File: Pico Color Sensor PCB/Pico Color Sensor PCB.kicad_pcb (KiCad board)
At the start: 2 copper layers, 62.2 x 80.4 mm, 13 parts

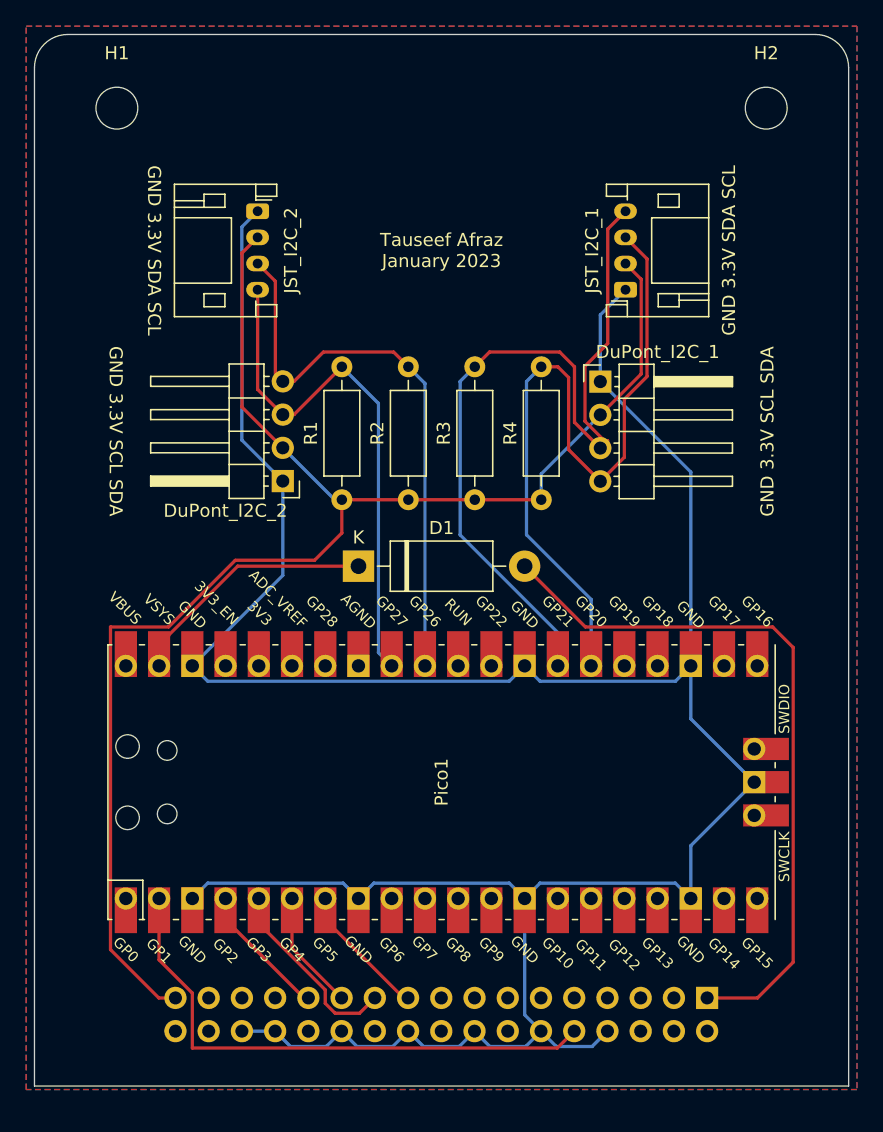
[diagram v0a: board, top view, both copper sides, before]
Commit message: Updated pinouts for JST
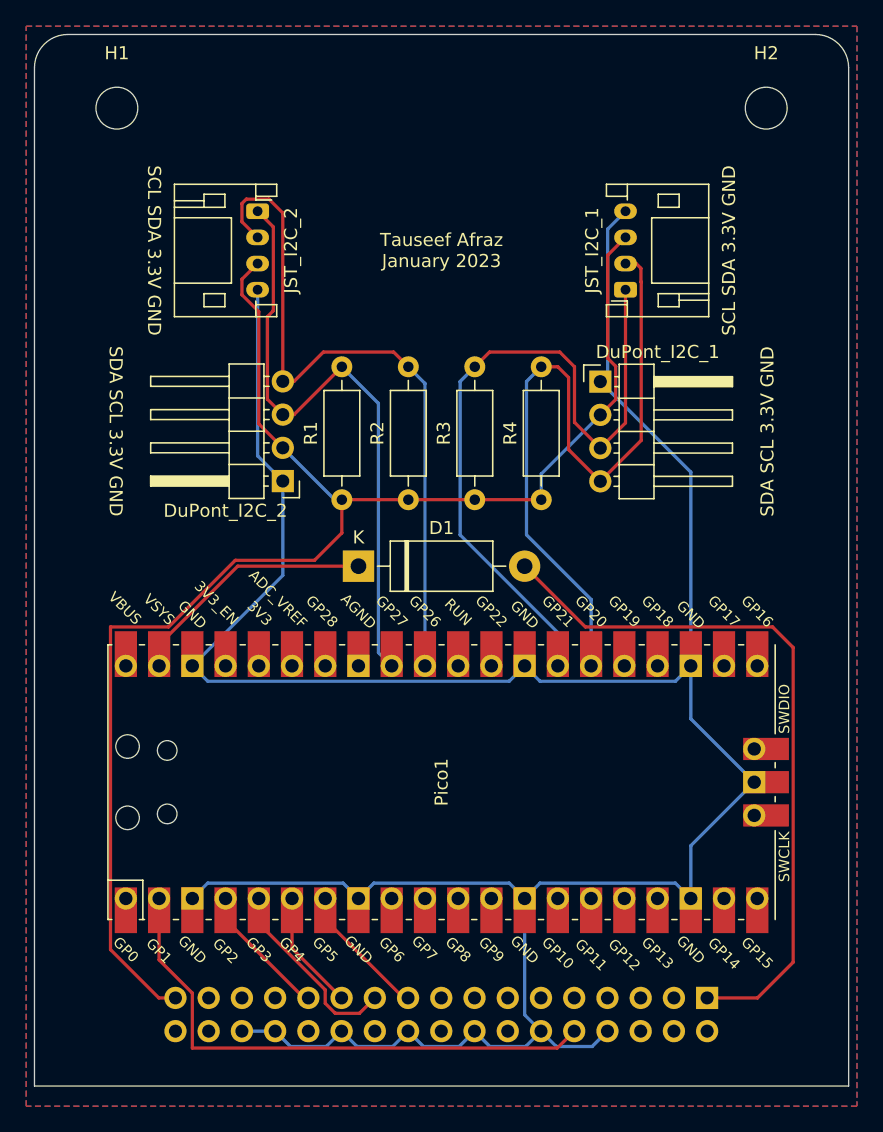
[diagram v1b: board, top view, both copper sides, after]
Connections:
- JST_I2C_1 pad 1: GND -> /SCL1
- JST_I2C_1 pad 2: +3.3V -> /SDA1
- JST_I2C_1 pad 3: /SDA1 -> +3.3V
- JST_I2C_1 pad 4: /SCL1 -> GND
- JST_I2C_2 pad 1: GND -> /SCL2
- JST_I2C_2 pad 2: +3.3V -> /SDA2
- JST_I2C_2 pad 3: /SDA2 -> +3.3V
- JST_I2C_2 pad 4: /SCL2 -> GND
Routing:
- net /SDA2: track 44.2 -> 54.0 mm
- net /SCL1: track 62.5 -> 54.9 mm
- net /SCL2: track 40.8 -> 47.2 mm
- net /SDA1: track 57.5 -> 55.7 mm
- net GND: track 218.1 -> 217.2 mm
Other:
- board text added: "SCL SDA 3.3V GND"
- board text added: "SDA SCL 3.3V GND"
- board text removed: "GND 3.3V SCL SDA"
- board text removed: "GND 3.3V SDA SCL"

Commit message: Updated text
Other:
- board text added: "Tauseef Afraz December 2022"
- board text removed: "Tauseef Afraz January 2023"
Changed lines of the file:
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@@
     (effects (font (size 1 1) (thickness 0.15)) (justify mirror))
   )
-  (gr_text "Tauseef Afraz\nJanuary 2023" (at 156.21 81.915) (layer "F.SilkS")
+  (gr_text "Tauseef Afraz\nDecember 2022" (at 156.21 81.915) (layer "F.SilkS")
     (effects (font (size 1 1) (thickness 0.15)))
   )

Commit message: Added V2 Text
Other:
- board text added: "Pico to Rio I2C Bridge PCB V2"
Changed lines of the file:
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@@
     (fp_line (start 7.25 0.25) (end -1.25 0.25) (layer "F.Fab") (width 0.1))
     (fp_line (start 7.95 -1.35) (end 7.25 -1.35) (layer "F.Fab") (width 0.1))
-    (pad "1" thru_hole roundrect locked (at 0 0 270) (size 1.2 1.75) (drill 0.75) (layers *.Cu *.Mask) (roundrect_rratio 0.208333)
+    (pad "1" thru_hole roundrect locked (at 0 0 270) (size 1.2 1.75) (drill 0.75) (layers *.Cu *.Mask) (roundrect_rratio 0.2083333333)
       (net 7 "/SCL2") (pinfunction "Pin_1") (pintype "passive"))
     (pad "2" thru_hole oval locked (at 2 0 270) (size 1.2 1.75) (drill 0.75) (layers *.Cu *.Mask)
@@
     (fp_line (start -1.25 -1.35) (end -1.95 -1.35) (layer "F.Fab") (width 0.1))
     (fp_line (start -1.95 6.25) (end 7.95 6.25) (layer "F.Fab") (width 0.1))
-    (pad "1" thru_hole roundrect locked (at 0 0 90) (size 1.2 1.75) (drill 0.75) (layers *.Cu *.Mask) (roundrect_rratio 0.208333)
+    (pad "1" thru_hole roundrect locked (at 0 0 90) (size 1.2 1.75) (drill 0.75) (layers *.Cu *.Mask) (roundrect_rratio 0.2083333333)
       (net 5 "/SCL1") (pinfunction "Pin_1") (pintype "passive"))
     (pad "2" thru_hole oval locked (at 2 0 90) (size 1.2 1.75) (drill 0.75) (layers *.Cu *.Mask)
@@
     (effects (font (size 1 1) (thickness 0.15)))
   )
+  (gr_text "Pico to Rio I2C Bridge PCB\nV2" (at 156.21 86.36) (layer "F.SilkS")
+    (effects (font (size 1 1) (thickness 0.15)))
+  )
